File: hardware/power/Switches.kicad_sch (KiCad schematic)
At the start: 72 parts, among them J101 Screw_Terminal_01x02, J102 Screw_Terminal_01x02, J105 Conn_02x03_Odd_Even, Q101 BSC093N15NS5, Q104 BSC093N15NS5, Q107 BSC093N15NS5, Q110 BSC093N15NS5, U101 UCC27211DDAR, U102 UCC27211DDAR, U105 INA283

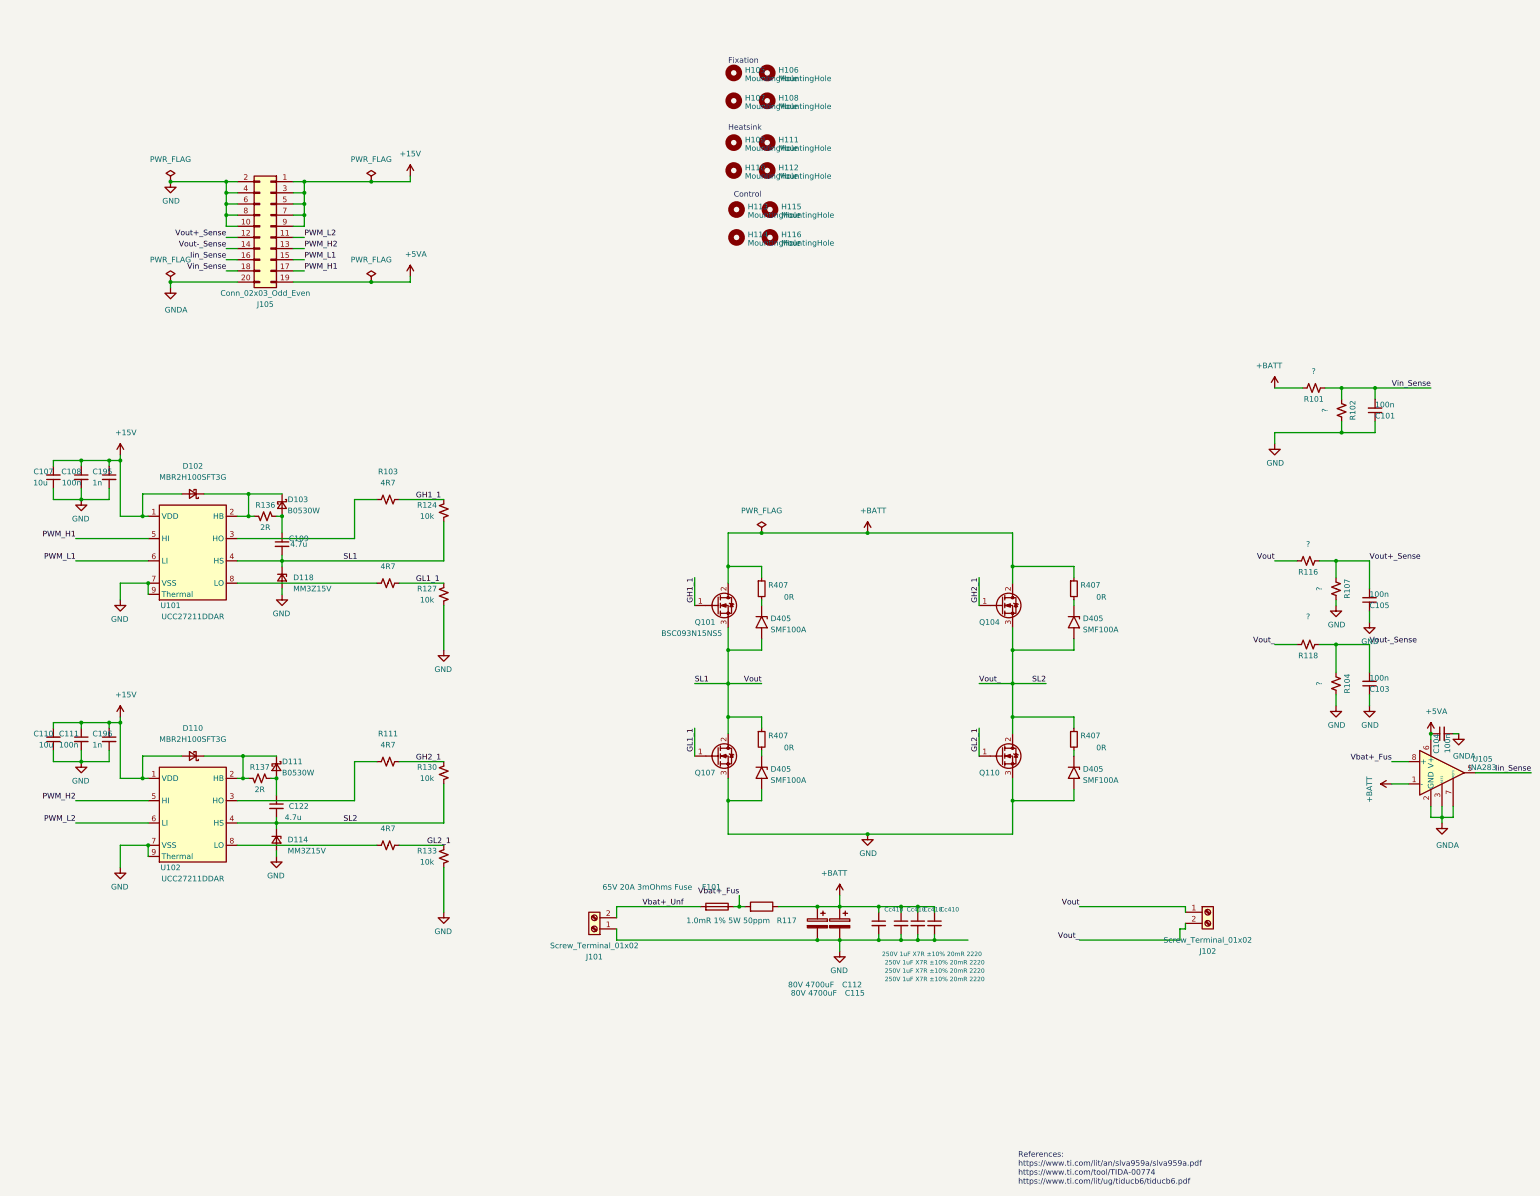
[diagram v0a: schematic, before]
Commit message: Organize schematics per domain
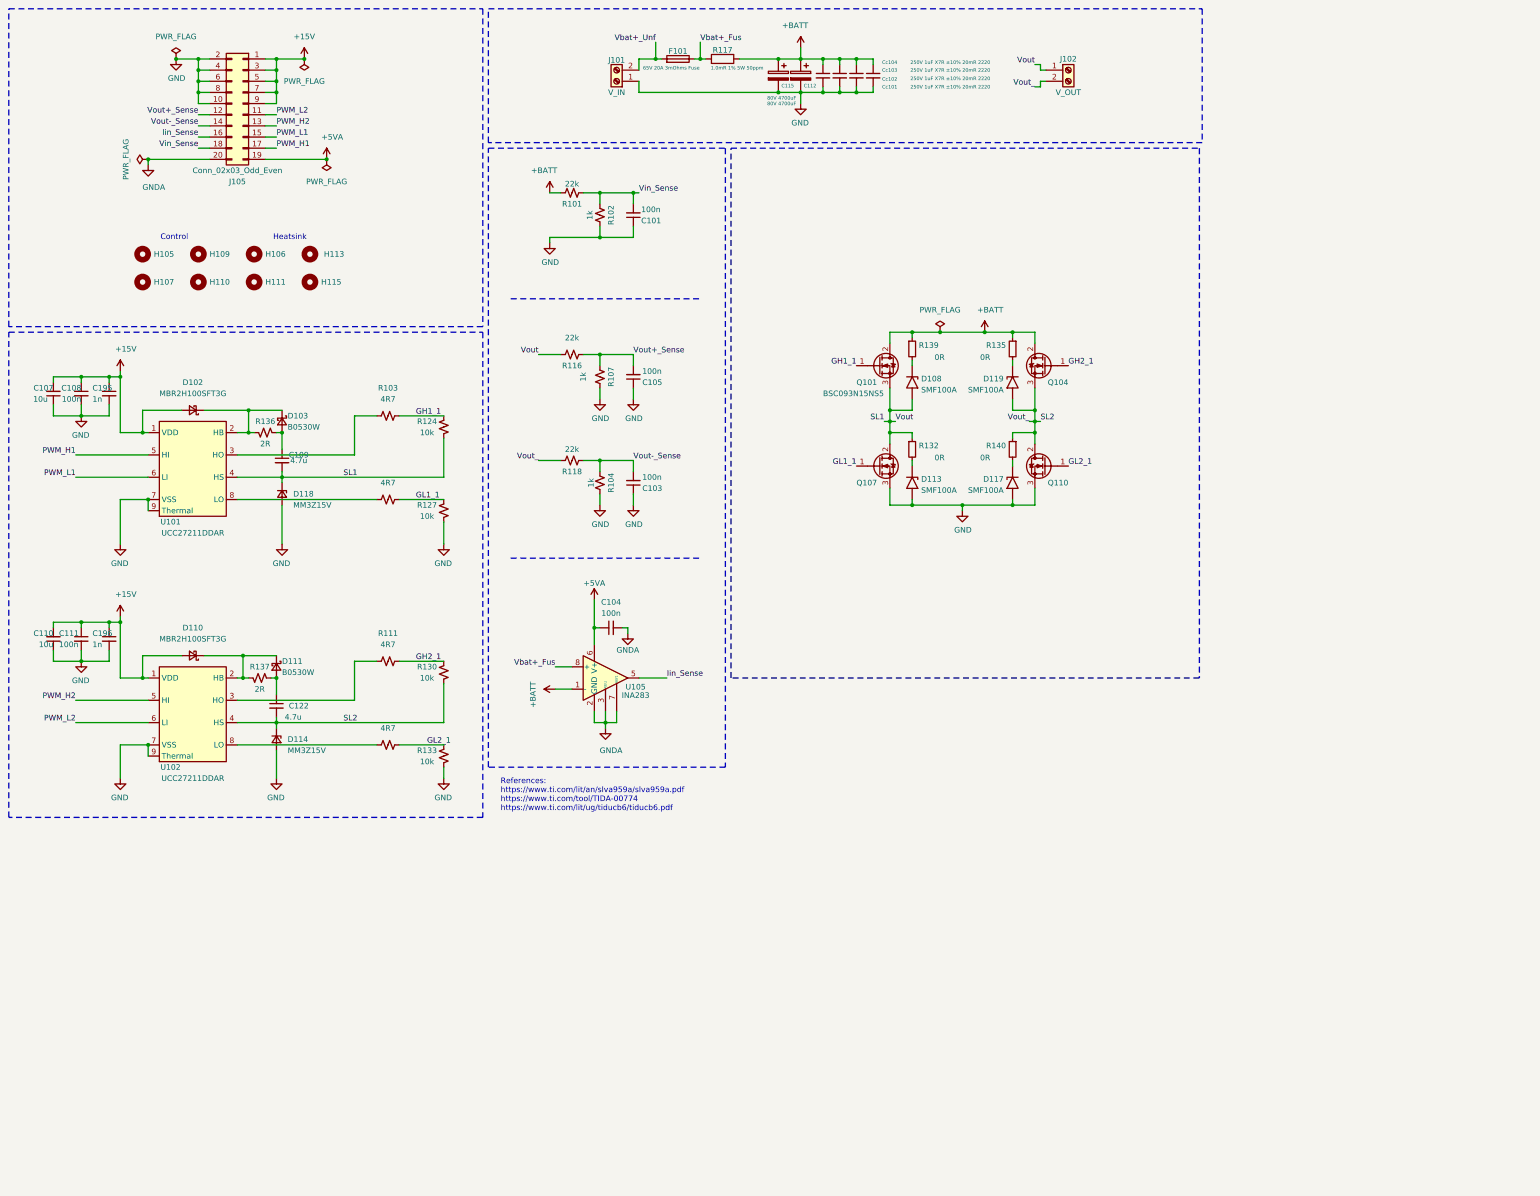
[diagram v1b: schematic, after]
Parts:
- removed H108, H112, H114, H116: MountingHole, MountingHole:MountingHole_3.5mm_Pad, symbol Mechanical:MountingHole
- J101: value Screw_Terminal_01x02 -> V_IN
- J102: value Screw_Terminal_01x02 -> V_OUT
- R101, R116, R118: value ? -> 22k
- R102, R104, R107: value ? -> 1k
- renumbered Cc410 to Cc101, Cc410 to Cc102, Cc410 to Cc103, Cc410 to Cc104, D405 to D108, D405 to D113, D405 to D117, D405 to D119, R407 to R132, R407 to R135, R407 to R139, R407 to R140
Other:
- note removed: "Fixation"
- company: (none) -> Zenite Solar
- title: (none) -> Módulo Direção Eletrônica 2025 (MDE25)
- moved on the sheet: C101, C103, C105, C107, C108, C109, C110, C111, C112, C115, C122, C195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
